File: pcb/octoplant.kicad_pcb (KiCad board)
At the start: 2 copper layers, 15.2 x 152.9 mm, 28 parts, among them IC1 ATTINY824-SSFR, J1 Conn_01x03, SW1 SW_Push

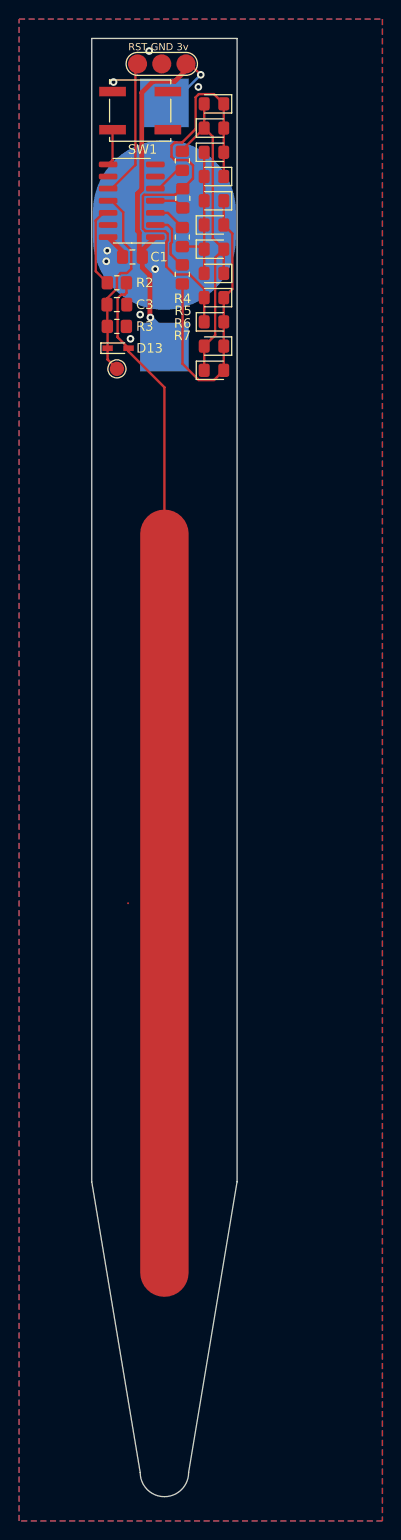
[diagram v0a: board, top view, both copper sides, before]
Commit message: Add silkscreen art
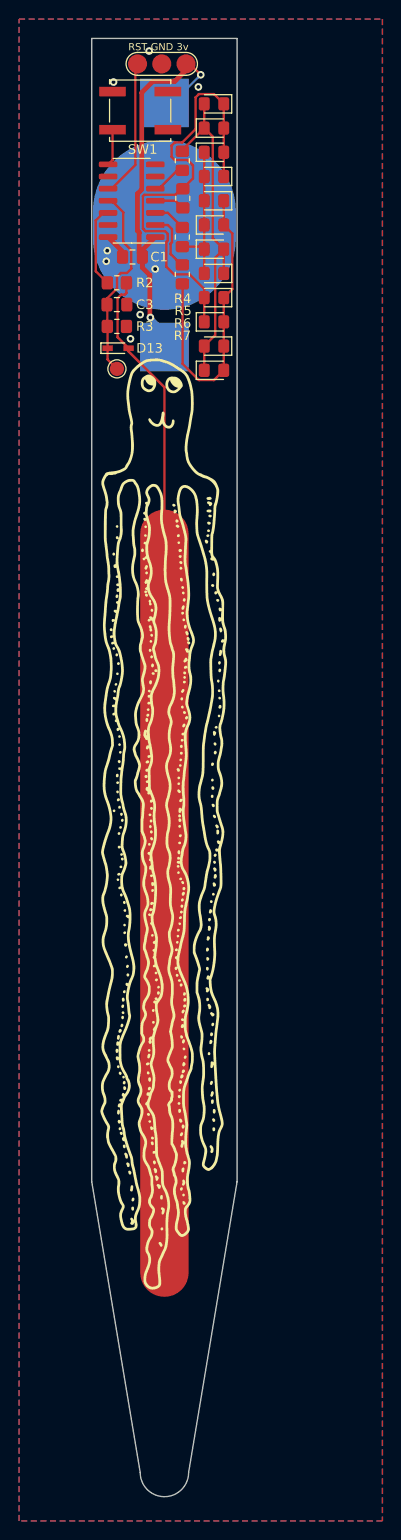
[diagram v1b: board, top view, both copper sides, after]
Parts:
- added G***: LOGO, art:art, F.Cu at (103.6, 98.9)

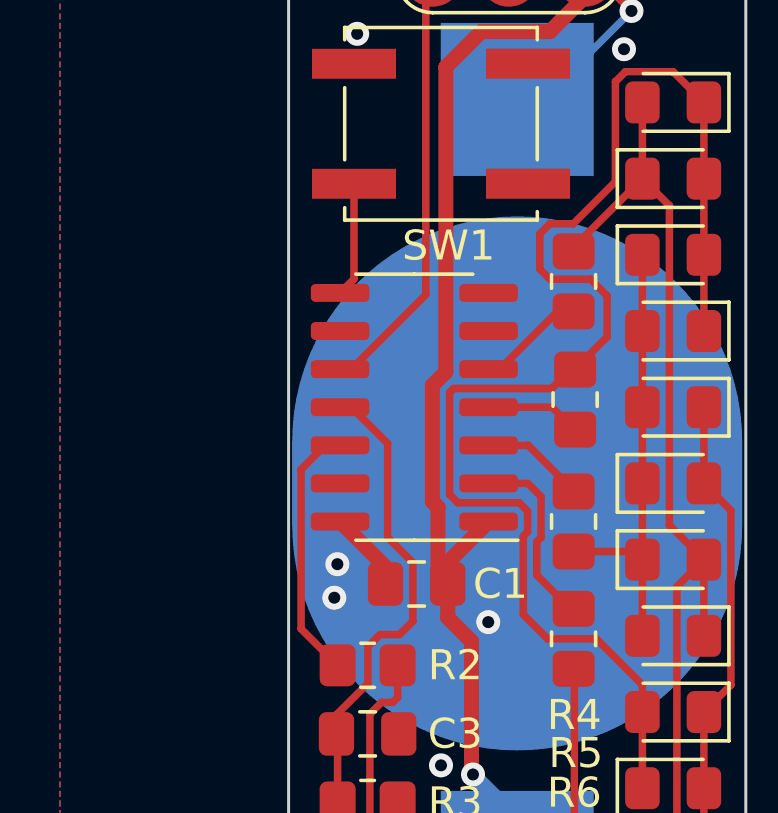
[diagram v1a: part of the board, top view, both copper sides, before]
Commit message: Change button pin to a fully async one
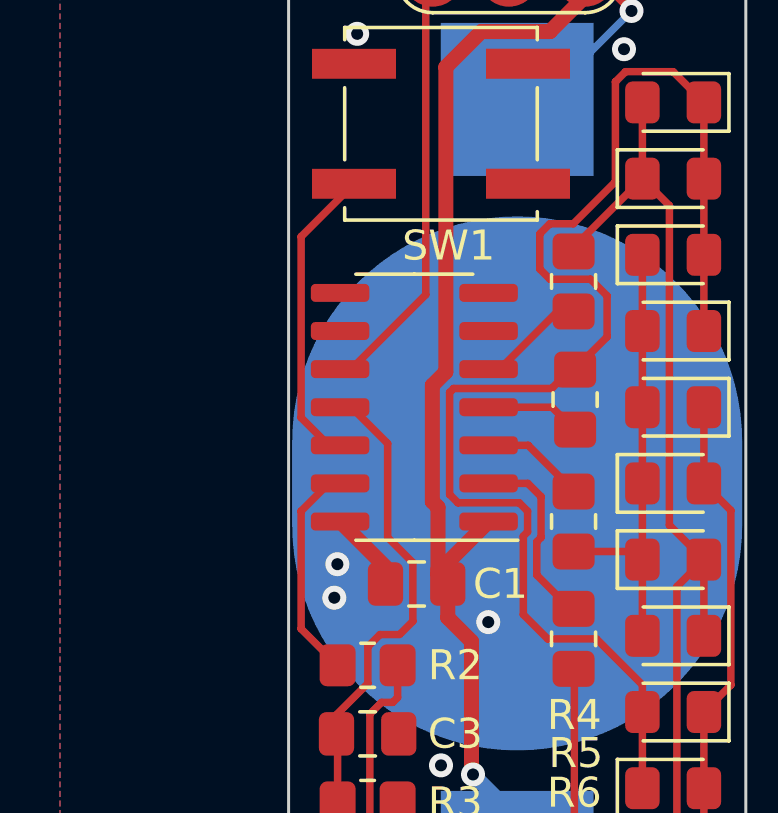
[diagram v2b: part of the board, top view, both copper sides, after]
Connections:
- IC1 pad 12: Sensor Input -> BTN
- IC1 pad 13: unconnected-(IC1-Pad13) -> Sensor Input
- IC1 pad 8: /BTN -> unconnected-(IC1-Pad8)
- SW1 pad 2: /BTN -> BTN
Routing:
- net BTN: track 0.00 -> 10.2 mm
- net /BTN: track 3.53 -> 0.00 mm
- net Sensor Input: track 8.67 -> 7.33 mm

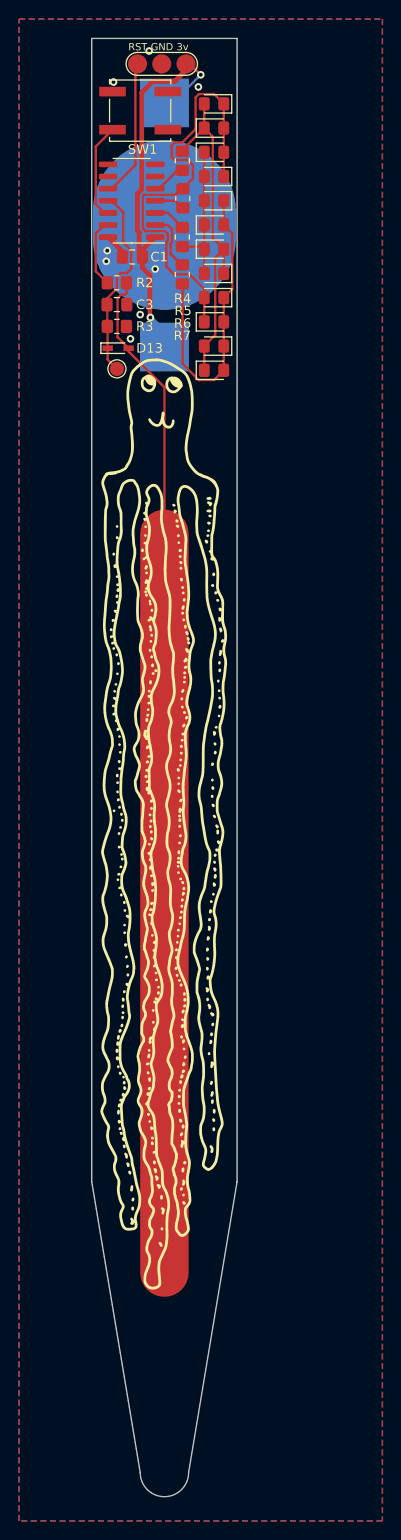
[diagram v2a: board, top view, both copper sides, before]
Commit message: resize capacitor pad
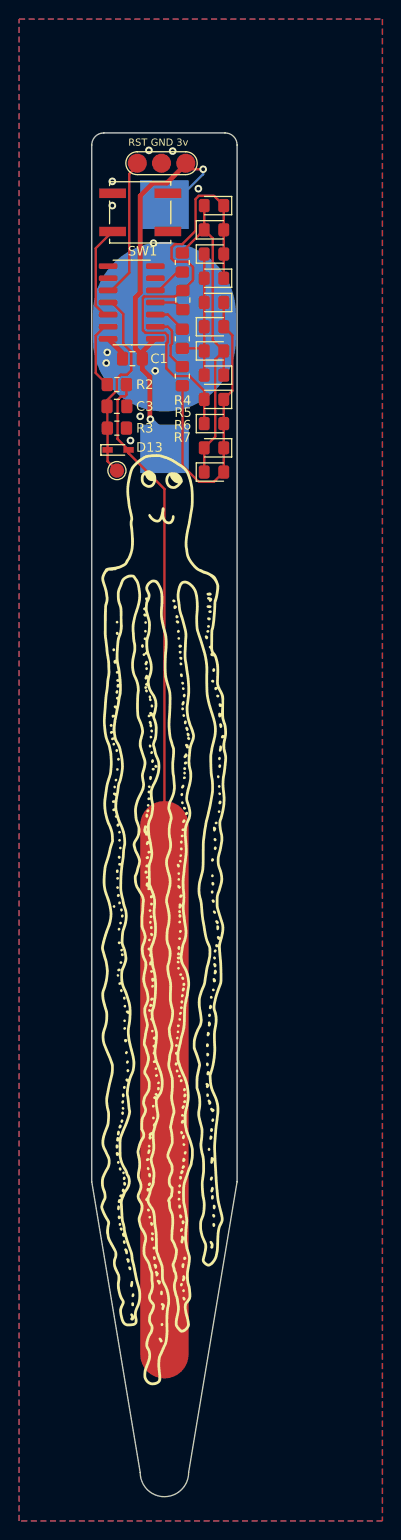
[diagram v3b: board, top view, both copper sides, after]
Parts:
- moved C2 19.6 mm to (104.1, 137.7)
- moved C1 10.7 mm to (100.8, 61.0)
- moved D11 10.7 mm to (109.3, 70.4)
- moved D4 10.7 mm to (109.3, 52.6)
- moved D9 10.7 mm to (109.3, 65.3)
- moved BT1 10.7 mm to (104.1, 57.7)
- moved C3 10.7 mm to (99.2, 66.0)
- moved D1 10.7 mm to (109.3, 45.0)
- moved D10 10.7 mm to (109.3, 67.8)
- moved D12 10.7 mm to (109.3, 72.9)
- moved D13 10.7 mm to (99.3, 70.6)
- moved D2 10.7 mm to (109.3, 47.5)
- moved D3 10.7 mm to (109.3, 50.0)
- moved D5 10.7 mm to (109.3, 55.1)
- moved D6 10.7 mm to (109.3, 57.7)
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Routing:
- net /C_Soil_+: track 67.7 -> 69.7 mm
- net VDD: track 41.7 -> 43.1 mm
- net GND: vias 8 -> 11
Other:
- board size 15.2 x 152.9 mm -> 15.2 x 143 mm
- board text added: "JLCJLCJLCJLC"
- board text added: "octo_plant_friend rev 1.0 03/22"
- board text removed: "octo_plant_friend rev 1.0"
